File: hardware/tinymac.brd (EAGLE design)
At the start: 43 x 41.4 mm, 29 parts, among them IC1 LPC1114FN28, J1 ZX62-B-5PA, SW1 TACT_SW, SW2 TACT_SW, SW3 TACT_SW, SW4 TACT_SW, SW5 TACT_SW, T1 TA48M033F

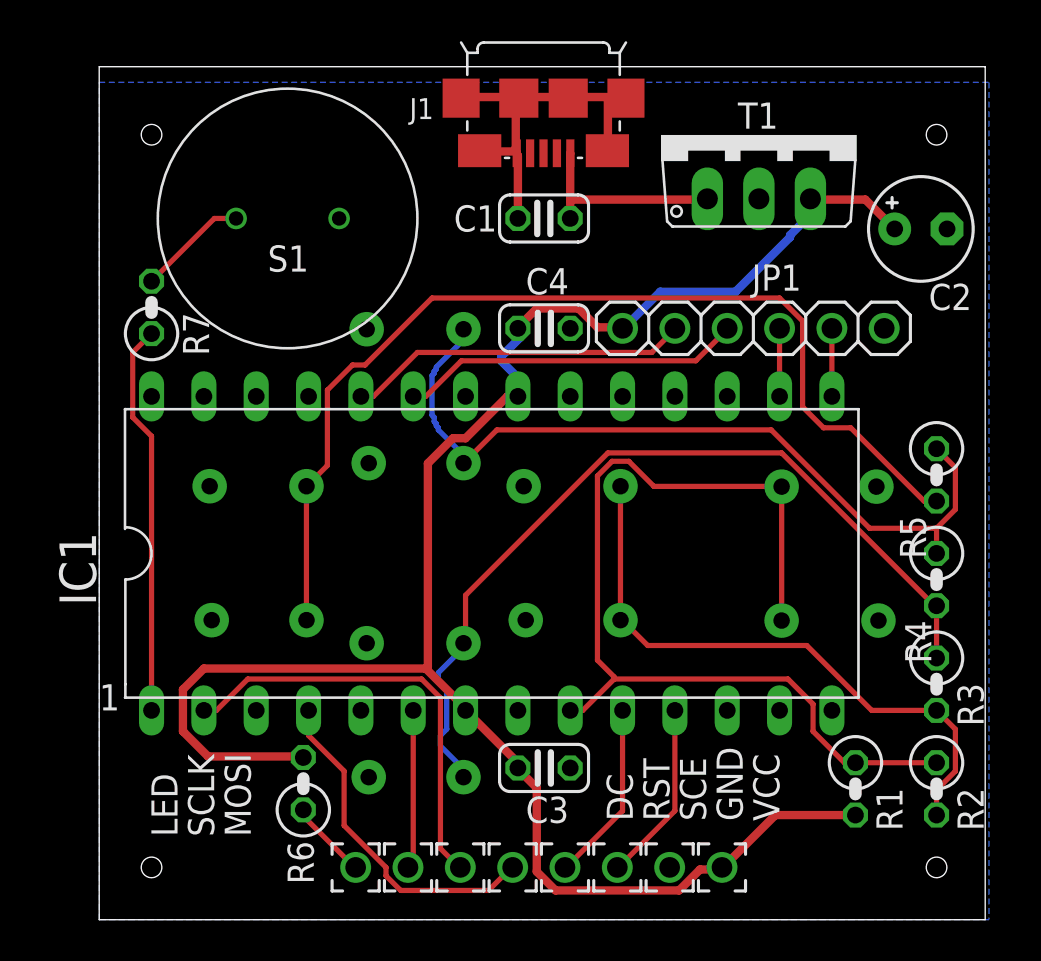
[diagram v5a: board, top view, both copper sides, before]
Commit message: adjust route and add restrict area around screw hole
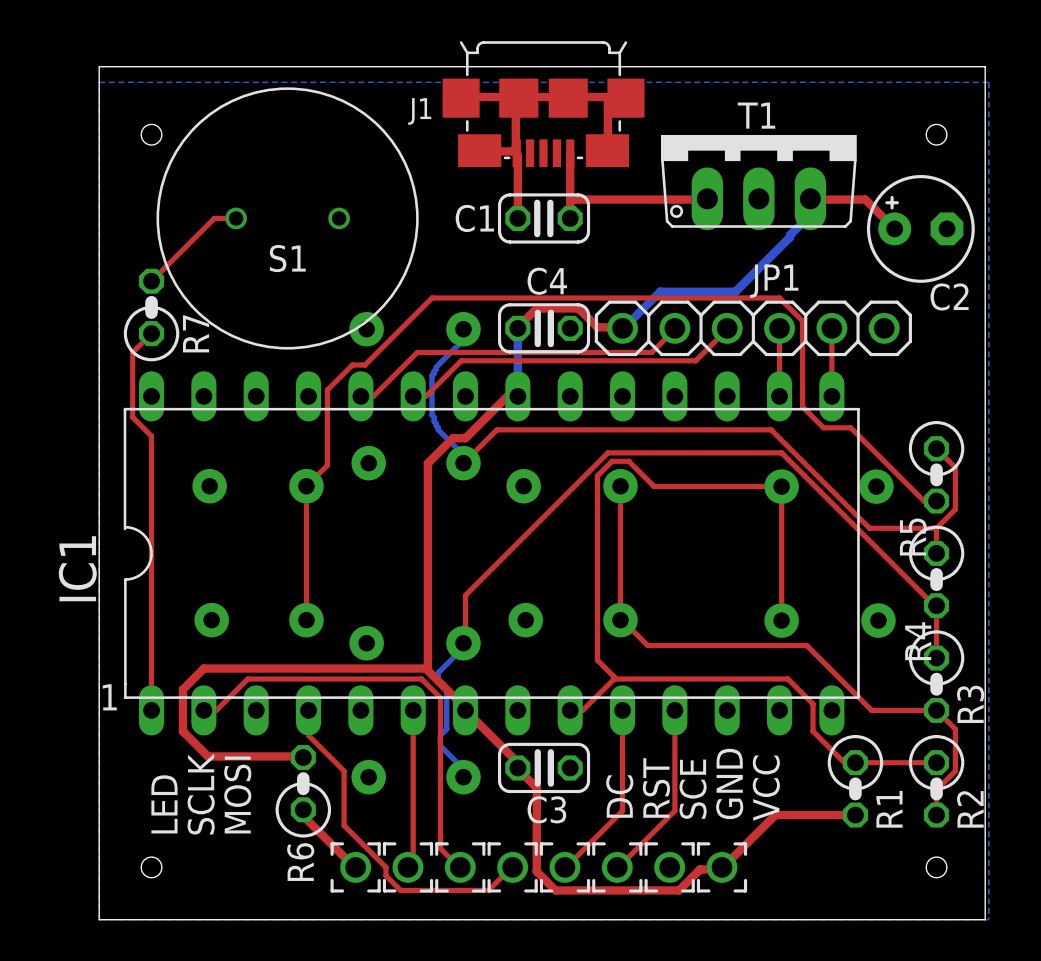
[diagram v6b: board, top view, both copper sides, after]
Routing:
- net +3.3V: track 92.8 -> 92.0 mm
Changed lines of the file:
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@@
 <hole x="2.54" y="38.1" drill="1"/>
 <hole x="40.64" y="38.1" drill="1"/>
+<circle x="2.54" y="2.54" radius="1.524" width="0.4064" layer="41"/>
+<circle x="40.64" y="2.54" radius="1.524" width="0.4064" layer="41"/>
+<circle x="40.64" y="38.1" radius="1.524" width="0.4064" layer="41"/>
+<circle x="2.54" y="38.1" radius="1.524" width="0.4064" layer="41"/>
 </plain>
 <attributes>
@@
 <wire x1="38.608" y1="33.528" x2="37.1856" y2="34.9504" width="0.4064" layer="1"/>
 <wire x1="34.544" y1="34.9504" x2="34.516" y2="34.988" width="0.4064" layer="1"/>
-<wire x1="20.32" y1="26.3144" x2="20.32" y2="25.4" width="0.4064" layer="16"/>
-<wire x1="19.5072" y1="27.1272" x2="20.32" y2="26.3144" width="0.4064" layer="16"/>
-<wire x1="19.5072" y1="27.3304" x2="19.5072" y2="27.1272" width="0.4064" layer="16"/>
-<wire x1="20.4216" y1="28.2448" x2="19.5072" y2="27.3304" width="0.4064" layer="16"/>
-<wire x1="20.4216" y1="28.5496" x2="20.4216" y2="28.2448" width="0.4064" layer="16"/>
-<wire x1="20.32" y1="28.6512" x2="20.4216" y2="28.5496" width="0.4064" layer="16"/>
-<wire x1="20.32" y1="28.6512" x2="20.32" y2="28.702" width="0.4064" layer="16"/>
 <wire x1="24.1808" y1="28.7528" x2="25.4" y2="28.7528" width="0.4064" layer="1"/>
 <wire x1="23.2664" y1="29.6672" x2="24.1808" y2="28.7528" width="0.4064" layer="1"/>
@@
 <wire x1="15.9512" y1="12.2936" x2="15.9512" y2="22.1488" width="0.4064" layer="1"/>
 <wire x1="15.9512" y1="12.2936" x2="15.8496" y2="12.192" width="0.4064" layer="1"/>
+<wire x1="20.32" y1="28.702" x2="20.32" y2="25.4" width="0.4064" layer="16"/>
 </signal>
 <signal name="VBUS" class="1">
@@
 <wire x1="10.0584" y1="20.9296" x2="10.06" y2="21.04" width="0.254" layer="1"/>
 </signal>
-<signal name="N$19">
+<signal name="N$19" class="2">
 <contactref element="LED" pad="1"/>
 <contactref element="R6" pad="1"/>
 <wire x1="9.9568" y1="4.9784" x2="9.9568" y2="5.2832" width="0.254" layer="1"/>
-<wire x1="12.3952" y1="2.54" x2="9.9568" y2="4.9784" width="0.254" layer="1"/>
+<wire x1="12.3952" y1="2.54" x2="9.9568" y2="4.9784" width="0.4064" layer="1"/>
 <wire x1="9.9568" y1="5.2832" x2="9.906" y2="5.334" width="0.254" layer="1"/>
 <wire x1="12.3952" y1="2.54" x2="12.446" y2="2.54" width="0.254" layer="1"/>

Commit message: change eagleup output setting
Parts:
- moved C1 0.76 mm to (21.6, 34.8)
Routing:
- net GND: track 19.3 -> 18.6 mm
- net VBUS: track 9.83 -> 9.31 mm
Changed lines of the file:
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@@
 <setting verticaltext="up"/>
 </settings>
-<grid distance="0.1" unitdist="inch" unit="inch" style="lines" multiple="1" display="yes" altdistance="0.01" altunitdist="inch" altunit="inch"/>
+<grid distance="0.1" unitdist="inch" unit="mm" style="lines" multiple="1" display="yes" altdistance="0.01" altunitdist="inch" altunit="inch"/>
 <layers>
 <layer number="1" name="Top" color="4" fill="1" visible="yes" active="yes"/>
@@
 <attribute name="NAME" x="31" y="38.3928" size="1.27" layer="25" ratio="10"/>
 </element>
-<element name="C1" library="tinymac" package="C025-024X044" value="0.1uF" x="21.59" y="34.036" smashed="yes" rot="R180">
-<attribute name="NAME" x="19.304" y="34.671" size="1.27" layer="25" ratio="10" rot="R180"/>
+<element name="C1" library="tinymac" package="C025-024X044" value="0.1uF" x="21.59" y="34.798" smashed="yes" rot="R180">
+<attribute name="NAME" x="19.304" y="35.433" size="1.27" layer="25" ratio="10" rot="R180"/>
 </element>
 <element name="C2" library="tinymac" package="E2,5-5" value="47uF" x="39.878" y="33.528" smashed="yes">
@@
 <attribute name="NAME" x="9.282" y="11.794" size="1.27" layer="26" rot="MR0"/>
 </element>
-<element name="R1" library="tinymac" package="0207/2V" value="10K" x="36.703" y="6.35" rot="R270"/>
-<element name="R2" library="tinymac" package="0207/2V" value="2.4K" x="40.64" y="6.35" rot="R270"/>
-<element name="R3" library="tinymac" package="0207/2V" value="4.3K" x="40.64" y="11.43" rot="R270"/>
+<element name="R1" library="tinymac" package="0207/2V" value="10K" x="36.703" y="6.35" smashed="yes" rot="R270">
+<attribute name="NAME" x="37.719" y="7.1628" size="1.27" layer="25" ratio="10" rot="R270"/>
+</element>
+<element name="R2" library="tinymac" package="0207/2V" value="2.4K" x="40.64" y="6.35" smashed="yes" rot="R270">
+<attribute name="NAME" x="41.402" y="7.1628" size="1.27" layer="25" ratio="10" rot="R270"/>
+</element>
+<element name="R3" library="tinymac" package="0207/2V" value="4.3K" x="40.64" y="11.43" smashed="yes" rot="R270">
+<attribute name="NAME" x="37.592" y="13.0048" size="1.27" layer="25" ratio="10" rot="R270"/>
+</element>
 <element name="R4" library="tinymac" package="0207/2V" value="8.2K" x="40.64" y="16.51" smashed="yes" rot="R270">
-<attribute name="NAME" x="39.116" y="14.5288" size="1.27" layer="25" ratio="10" rot="R270"/>
+<attribute name="NAME" x="37.592" y="18.3388" size="1.27" layer="25" ratio="10" rot="R270"/>
 </element>
 <element name="R5" library="tinymac" package="0207/2V" value="24K" x="40.64" y="21.59" smashed="yes" rot="R270">
-<attribute name="NAME" x="38.862" y="19.6088" size="1.27" layer="25" ratio="10" rot="R270"/>
+<attribute name="NAME" x="37.592" y="25.4508" size="1.27" layer="25" ratio="10" rot="R270"/>
 </element>
 <element name="C4" library="tinymac" package="C025-024X044" value="0.1uF" x="21.59" y="28.702" smashed="yes">
@@
 <wire x1="20.2184" y1="37.4904" x2="20.264" y2="37.2" width="0.4064" layer="1"/>
 <wire x1="20.2184" y1="39.7256" x2="20.364" y2="39.875" width="0.4064" layer="1"/>
-<wire x1="20.32" y1="34.036" x2="20.32" y2="37.084" width="0.4064" layer="1"/>
 <wire x1="20.32" y1="37.084" x2="20.264" y2="37.2" width="0.4064" layer="1"/>
+<wire x1="20.32" y1="37.084" x2="20.32" y2="34.798" width="0.4064" layer="1"/>
 </signal>
 <signal name="N$15">
@@
 <contactref element="T1" pad="1"/>
 <contactref element="C1" pad="1"/>
-<wire x1="22.86" y1="34.036" x2="22.86" y2="34.9504" width="0.4064" layer="1"/>
-<wire x1="22.86" y1="34.9504" x2="22.86" y2="37.1856" width="0.4064" layer="1"/>
 <wire x1="22.86" y1="37.1856" x2="22.864" y2="37.2" width="0.4064" layer="1"/>
-<wire x1="22.86" y1="34.9504" x2="29.464" y2="34.9504" width="0.4064" layer="1"/>
 <wire x1="29.464" y1="34.9504" x2="29.516" y2="34.988" width="0.4064" layer="1"/>
+<wire x1="22.86" y1="37.1856" x2="22.86" y2="34.798" width="0.4064" layer="1"/>
+<wire x1="22.86" y1="34.798" x2="29.516" y2="34.798" width="0.4064" layer="1"/>
+<wire x1="29.516" y1="34.798" x2="29.516" y2="34.988" width="0.4064" layer="1"/>
 </signal>
 <signal name="N$2">

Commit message: change DRU setting to Seeed-2layer-DRU
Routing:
- net N$7: track 39.2 -> 51.9 mm
- net +3.3V: track 92.0 -> 89.6 mm
- net N$8: track 49.5 -> 51.2 mm
